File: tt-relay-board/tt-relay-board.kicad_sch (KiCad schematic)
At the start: 18 parts, among them J1 AC_IN, J2 Screw_Terminal_01x02, J4 Relays, J5 Conn_02x11_Odd_Even, J7 AudioJack4_SwitchR1, J8 AudioJack4_SwitchR1, Q1 Q_NPN_EBC

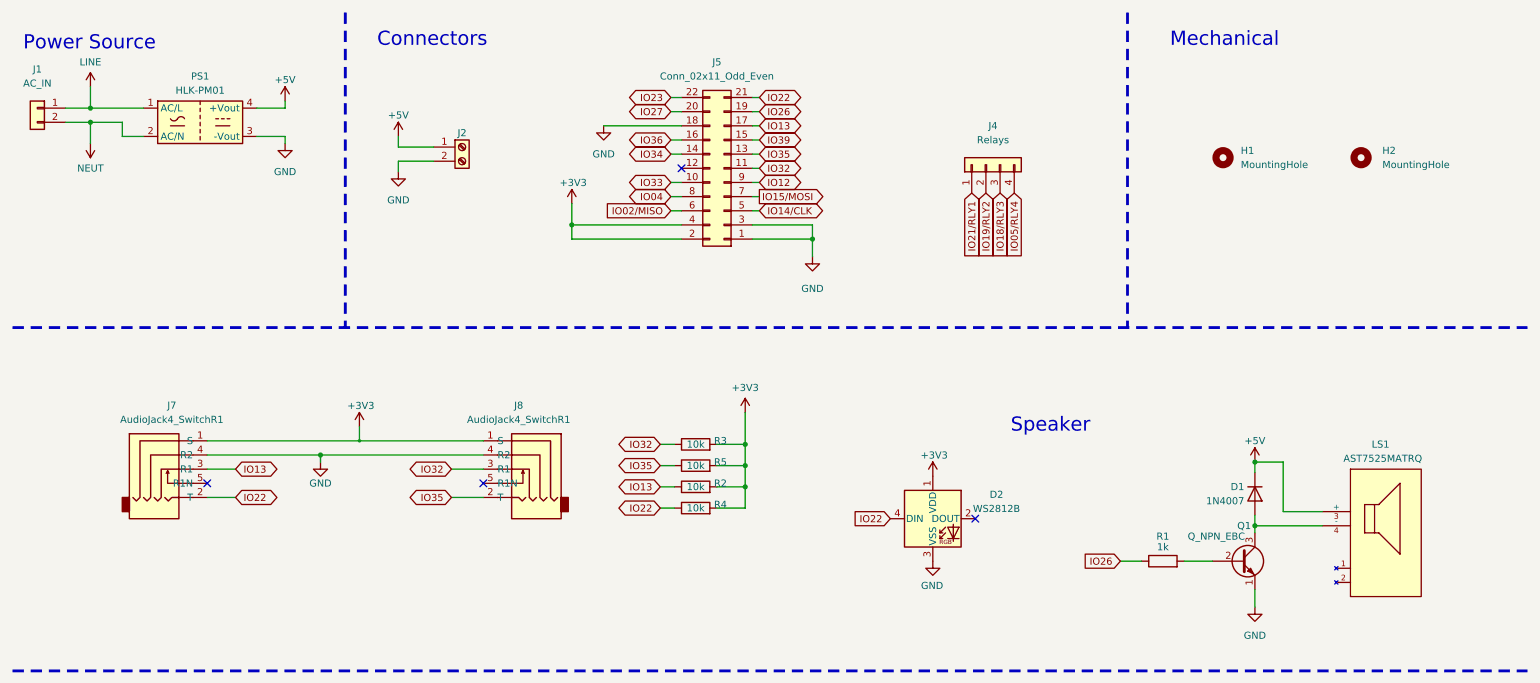
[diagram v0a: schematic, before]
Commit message: Fix component positions in tt-relay-board
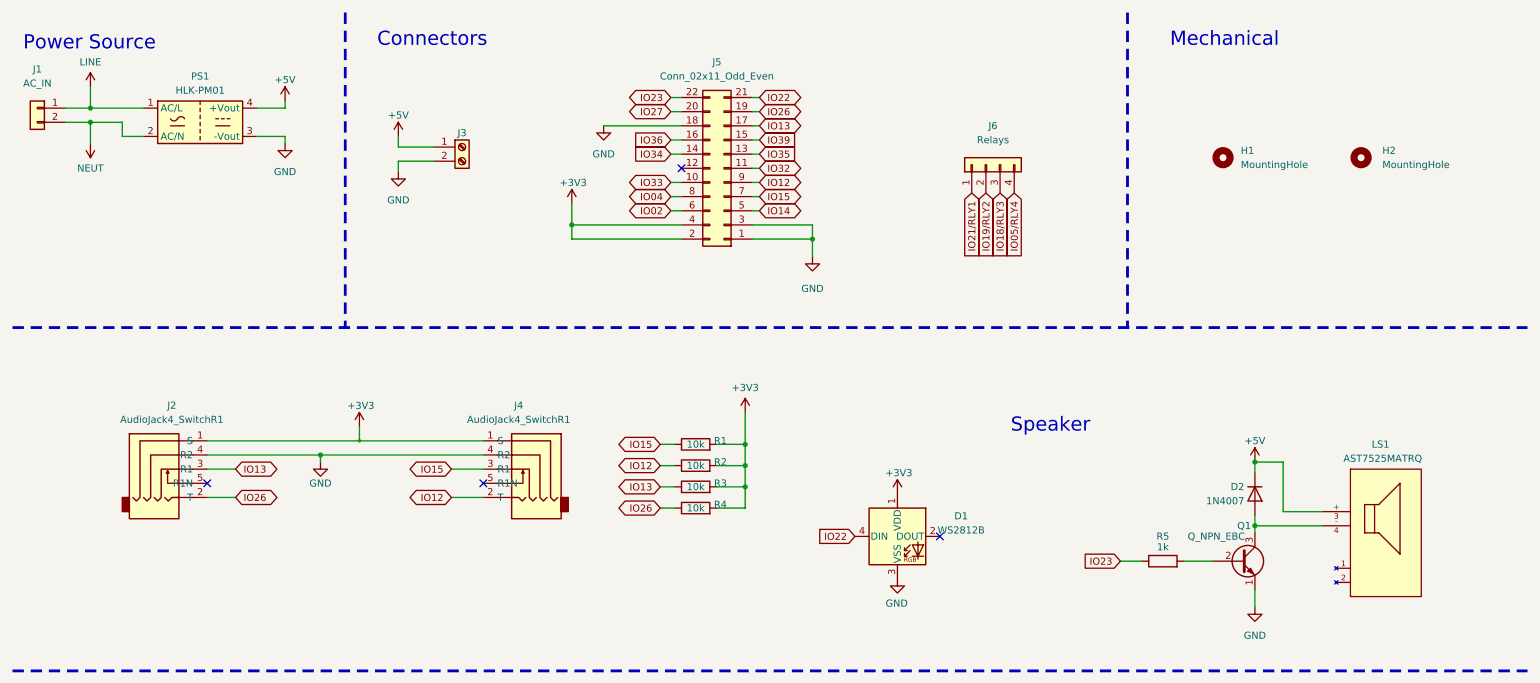
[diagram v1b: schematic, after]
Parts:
- removed D2: WS2812B, reptile-monitor:LED_WS2812B_PLCC4_5.0x5.0mm_P3.2mm, symbol LED:WS2812B
- added D1: WS2812B, tt-relay-board:LED_WS2812B_PLCC4_5.0x5.0mm_P3.2mm, symbol tt-relay-board:WS2812B
- J2: renamed from J7; footprint reptile-monitor:Korean Hroparts Elec PJ-227-5A -> tt-relay-board:Korean Hroparts Elec PJ-227-5A
- J4: renamed from J8; footprint reptile-monitor:Korean Hroparts Elec PJ-227-5A -> tt-relay-board:Korean Hroparts Elec PJ-227-5A
- LS1: footprint reptile-monitor:Mallory_Sonalert_Products_Inc-AST7525MATRQ-0-0-MFG -> tt-relay-board:Mallory_Sonalert_Products_Inc-AST7525MATRQ-0-0-MFG
- PS1: footprint reptile-monitor-power:Converter_ACDC_HiLink_HLK-PMxx -> tt-relay-board:Converter_ACDC_HiLink_HLK-PMxx
- Q1: footprint Package_TO_SOT_THT:TO-92_Inline_Wide -> Package_TO_SOT_THT:TO-92_Inline
- renumbered D1 to D2, J2 to J3, J4 to J6, R3 to R1, R5 to R2, R2 to R3, R1 to R5
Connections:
- net +3V3: now also D1.1 (VDD)
- net GND: now also D1.3 (VSS)
- net IO12: now also J4.2 (T), R2.1
- net IO22: now also D1.4 (DIN); no longer J2.2 (T), R4.1
- net IO23: now also R5.1
- net IO26: now also J2.2 (T), R4.1; no longer R5.1
- net IO32: no longer J4.3 (R1), R1.1
- net IO35: no longer J4.2 (T), R2.1
- net IO02/MISO renamed IO02
- net IO14/CLK renamed IO14
- net IO15/MOSI renamed IO15
- net IO15: now also J4.3 (R1), R1.1
